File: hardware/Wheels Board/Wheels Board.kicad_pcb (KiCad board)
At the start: 2 copper layers, 224.7 x 101.3 mm, 45 parts, among them J1 Conn_01x05, J10 gnd, J2 24v, J3 Conn_01x03, J4 53307-2471, J5 Conn_01x02, J6 Conn_01x05_Pin, J7 Conn_01x07, J8 Conn_01x03, J9 5v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

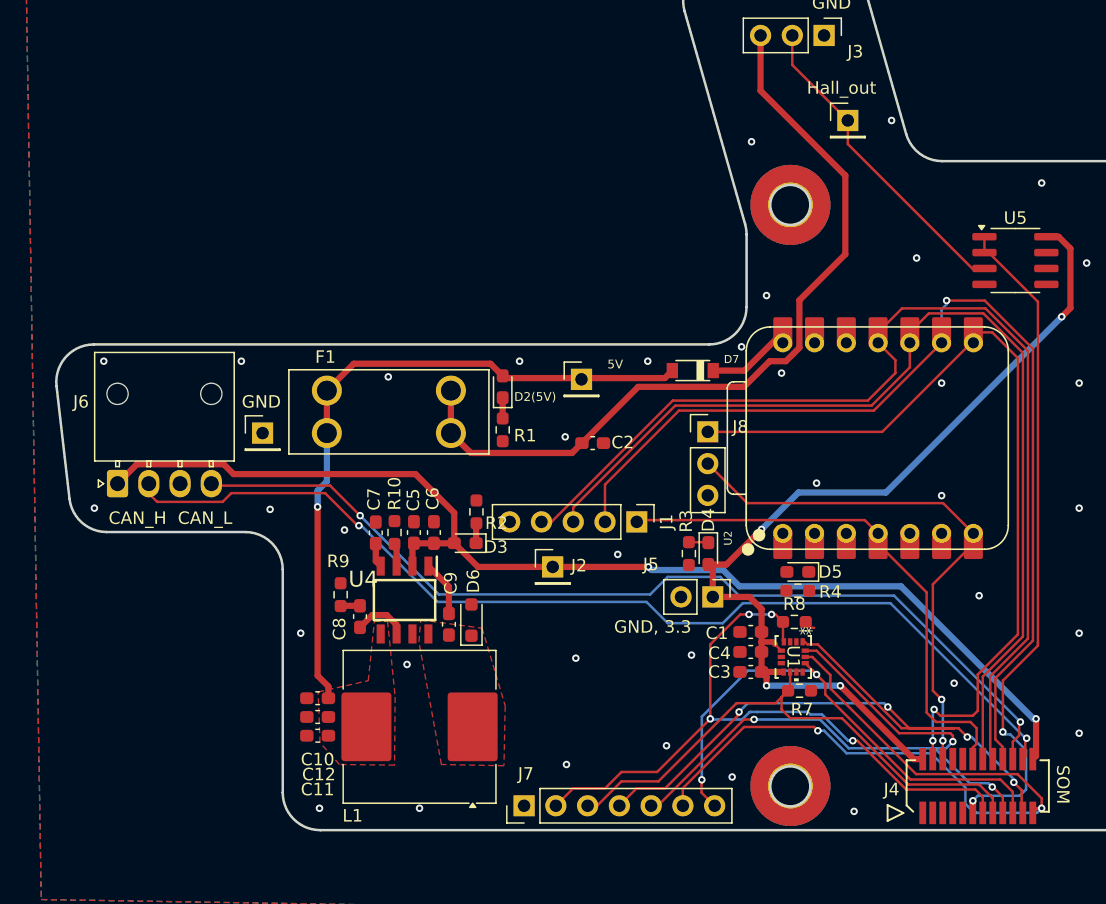
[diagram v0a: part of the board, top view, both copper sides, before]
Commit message: silkscreen final
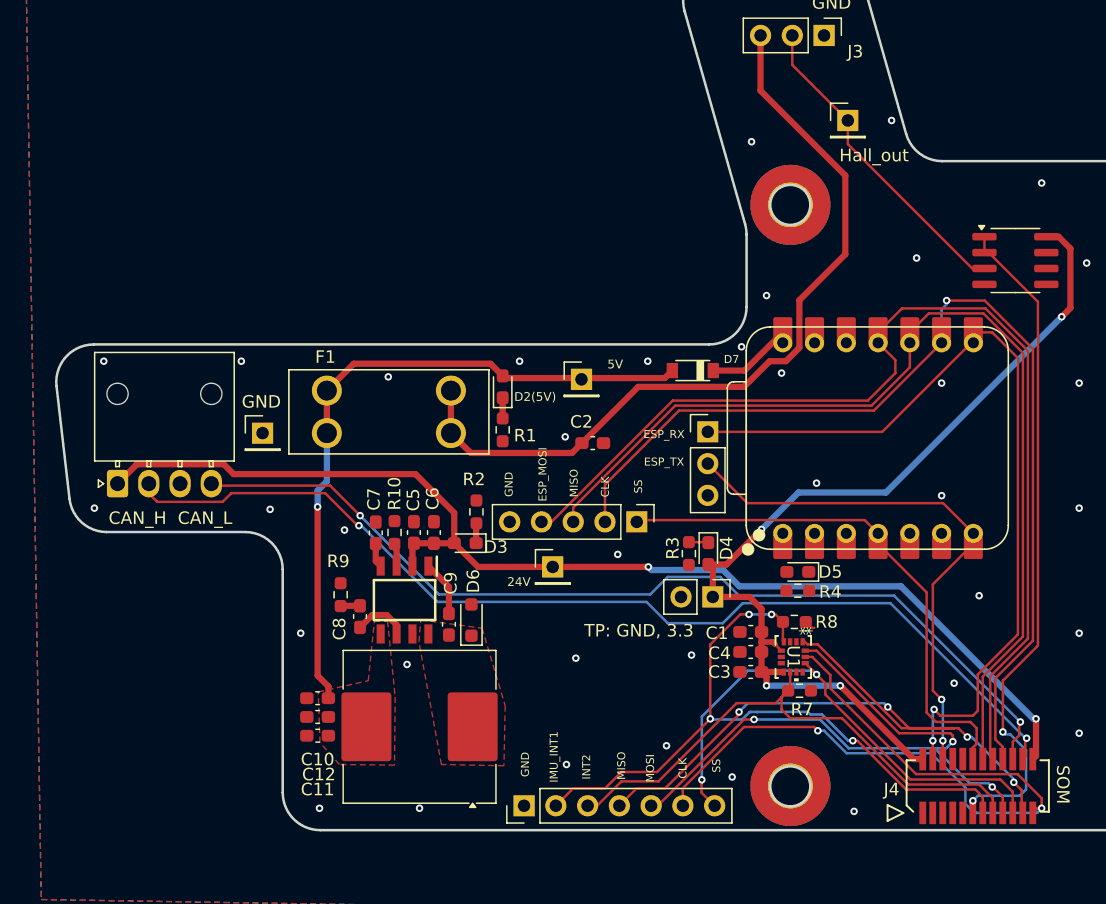
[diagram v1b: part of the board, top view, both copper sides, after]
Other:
- board text added: "24V"
- board text added: "CLK"
- board text added: "ESP_MOSI"
- board text added: "ESP_RX"
- board text added: "ESP_TX"
- board text added: "IMU_INT1"
- board text added: "INT2"
- board text added: "MISO"
- board text added: "MOSI"
- board text added: "SS"
- board text added: "TP: GND, 3.3"
- board text removed: "GND, 3.3"
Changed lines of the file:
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@@
 		(tags "Through hole pin header THT 1x01 2.54mm single row")
 		(property "Reference" "Hall_out"
-			(at -0.5 -2.6 0)
+			(at 2.1 2.8 0)
 			(layer "F.SilkS")
 			(effects
@@
 		(tags "resistor handsolder")
 		(property "Reference" "R2"
-			(at -0.9 1.6 0)
+			(at 2.6 -0.2 0)
 			(layer "F.SilkS")
 			(effects
@@
 			(at 2.55 0.14 180)
 			(layer "F.SilkS")
+			(hide yes)
 			(effects
 				(font
@@
 			(at 6.54 -2.92 180)
 			(layer "F.SilkS")
+			(hide yes)
 			(effects
 				(font
@@
 			(at 2.1 -0.1 0)
 			(layer "F.SilkS")
+			(hide yes)
 			(effects
 				(font
@@
 			(at -2.6 4.95 180)
 			(layer "F.SilkS")
+			(hide yes)
 			(effects
 				(font
@@
 			(unlocked yes)
 			(layer "F.SilkS")
+			(hide yes)
 			(effects
 				(font
@@
 			(at -1.6625 3.300002 180)
 			(layer "F.SilkS")
+			(hide yes)
 			(effects
 				(font
@@
 		(tags "capacitor handsolder")
 		(property "Reference" "C2"
-			(at 2.4 -0.05 0)
+			(at -0.9 -1.7 0)
 			(layer "F.SilkS")
 			(effects
@@
 		(tags "resistor handsolder")
 		(property "Reference" "R8"
-			(at 0 -1.43 0)
+			(at 2.575001 0 0)
 			(layer "F.SilkS")
 			(effects
@@
 			(at 0 -3.4 0)
 			(layer "F.SilkS")
+			(hide yes)
 			(effects
 				(font
@@
 			(at 0 -2.38 90)
 			(layer "F.SilkS")
+			(hide yes)
 			(effects
 				(font
@@
 			(at 2.6 -0.4 0)
 			(layer "F.SilkS")
+			(hide yes)
 			(effects
 				(font
@@
 			(at 5.349999 -7.112501 180)
 			(layer "F.SilkS")
+			(hide yes)
 			(effects
 				(font
@@
 		(tags "resistor handsolder")
 		(property "Reference" "R3"
-			(at -2.594795 0.219267 90)
+			(at -0.435177 1.288604 90)
 			(layer "F.SilkS")
 			(effects
@@
 		(tags "LED handsolder")
 		(property "Reference" "D4"
-			(at -2.687006 0 90)
+			(at -0.435177 -1.455761 90)
 			(layer "F.SilkS")
 			(effects
@@
 		(layer "Edge.Cuts")
 	)
+	(gr_text "ESP_TX\n"
+		(at 101.8 76.3 0)
+		(layer "F.SilkS")
+		(effects
+			(font
+				(size 0.640597 0.640597)
+				(thickness 0.15)
+			)
+		)
+	)
 	(gr_text "5V"
 		(at 97.9 68.5 0)
@@
 	)
 	(gr_text "GND\n"
+		(at 89.4 78.1 90)
+		(layer "F.SilkS")
+		(effects
+			(font
+				(size 0.640597 0.640597)
+				(thickness 0.15)
+			)
+		)
+	)
+	(gr_text "GND\n"
 		(at 115.2 39.6 0)
 		(layer "F.SilkS")
@@
 		)
 	)
+	(gr_text "CLK"
+		(at 103.3 100.8 90)
+		(layer "F.SilkS")
+		(effects
+			(font
+				(size 0.640597 0.640597)
+				(thickness 0.15)
+			)
+		)
+	)
+	(gr_text "CLK\n"
+		(at 97.1 78.3 90)
+		(layer "F.SilkS")
+		(effects
+			(font
+				(size 0.640597 0.640597)
+				(thickness 0.15)
+			)
+		)
+	)
+	(gr_text "MOSI\n"
+		(at 100.7 100.8 90)
+		(layer "F.SilkS")
+		(effects
+			(font
+				(size 0.640597 0.640597)
+				(thickness 0.15)
+			)
+		)
+	)
+	(gr_text "GND\n"
+		(at 90.7 100.5 90)
+		(layer "F.SilkS")
+		(effects
+			(font
+				(size 0.640597 0.640597)
+				(thickness 0.15)
+			)
+		)
+	)
+	(gr_text "MISO\n"
+		(at 94.6 78 90)
+		(layer "F.SilkS")
+		(effects
+			(font
+				(size 0.640597 0.640597)
+				(thickness 0.15)
+			)
+		)
+	)
+	(gr_text "INT2"
+		(at 95.6 100.7 90)
+		(layer "F.SilkS")
+		(effects
+			(font
+				(size 0.640597 0.640597)
+				(thickness 0.15)
+			)
+		)
+	)
 	(gr_text "HALL"
 		(at 111.6 38.5 0)
@@
 		)
 	)
+	(gr_text "IMU_INT1\n"
+		(at 93 99.9 90)
+		(layer "F.SilkS")
+		(effects
+			(font
+				(size 0.640597 0.640597)
+				(thickness 0.15)
+			)
+		)
+	)
+	(gr_text "24V\n"
+		(at 90.2 85.9 0)
+		(layer "F.SilkS")
+		(effects
+			(font
+				(size 0.7 0.7)
+				(thickness 0.15)
+			)
+		)
+	)
+	(gr_text "SS"
+		(at 99.749133 78.268886 90)
+		(layer "F.SilkS")
+		(effects
+			(font
+				(size 0.640597 0.640597)
+				(thickness 0.15)
+			)
+		)
+	)
+	(gr_text "SS\n"
+		(at 106 100.6 90)
+		(layer "F.SilkS")
+		(effects
+			(font
+				(size 0.640597 0.640597)
+				(thickness 0.15)
+			)
+		)
+	)
+	(gr_text "MISO\n"
+		(at 98.4 100.6 90)
+		(layer "F.SilkS")
+		(effects
+			(font
+				(size 0.640597 0.640597)
+				(thickness 0.15)
+			)
+		)
+	)
+	(gr_text "ESP_RX\n"
+		(at 101.8 74.1 0)
+		(layer "F.SilkS")
+		(effects
+			(font
+				(size 0.640597 0.640597)
+				(thickness 0.15)
+			)
+		)
+	)
+	(gr_text "ESP_MOSI\n"
+		(at 92.1 77.3 90)
+		(layer "F.SilkS")
+		(effects
+			(font
+				(size 0.640597 0.640597)
+				(thickness 0.15)
+			)
+		)
+	)
 	(gr_text "CAN_L"
 		(at 65.1 80.8 0)
@@
 		)
 	)
-	(gr_text "GND, 3.3"
-		(at 100.9 89.5 0)
+	(gr_text "TP: GND, 3.3"
+		(at 99.8 89.8 0)
 		(layer "F.SilkS")
 		(effects
@@
 		(name "$teardrop_padvia$")
 		(hatch none 0.1)
-		(priority 30009)
+		(priority 30000)
 		(attr
 			(teardrop
@@
 		(name "$teardrop_padvia$")
 		(hatch none 0.1)
-		(priority 30010)
+		(priority 30007)
 		(attr
 			(teardrop
@@
 		(polygon
 			(pts
-				(xy 81.935001 83.55) (xy 81.435001 83.55) (xy 81.360001 83.875) (xy 81.685001 84.64) (xy 82.010001 83.875)
+				(xy 82.75 83.0625) (xy 82.75 82.5625) (xy 82.194869 82.3375) (xy 81.799 82.8125) (xy 82.194869 83.2875)
 			)
 		)
 	)
 	(zone
-		(net 3)
-		(net_name "+24V")
+		(net 45)
+		(net_name "/24v to 5v convertor/ROSC")
 		(layer "F.Cu")
 		(name "$teardrop_padvia$")
 		(hatch none 0.1)
-		(priority 30007)
+		(priority 30002)
 		(attr
 			(teardrop
@@
 		(polygon
 			(pts
-				(xy 82.75 83.0625) (xy 82.75 82.5625) (xy 82.194869 82.3375) (xy 81.799 82.8125) (xy 82.194869 83.2875)
+				(xy 80.665001 83.55) (xy 80.165001 83.55) (xy 80.090001 83.875) (xy 80.415001 84.64) (xy 80.740001 83.875)
 			)
 		)
@@
 	)
 	(zone
-		(net 9)
-		(net_name "+5V")
-		(layer "F.Cu")
-		(hatch edge 0.5)
-		(priority 4)
-		(connect_pads yes
-			(clearance 0.1)
-		)
-		(min_thickness 0.1)
-		(filled_areas_thickness no)
-		(fill yes
-			(thermal_gap 0.1)
-			(thermal_bridge_width 0.5)
-		)
-		(polygon
-			(pts
-				(xy 78.639835 89.05) (xy 79.695 89.05) (xy 80.3 95.1) (xy 80.25 100.55) (xy 75.843032 100.5) (xy 74.293032 98.75)
-				(xy 74.143032 94.7) (xy 78.15 93.8)
-			)
-		)
-	)
-	(zone
 		(net 7)
 		(net_name "Net-(U4-BOOT)")
@@
 		(name "$teardrop_padvia$")
 		(hatch none 0.1)
-		(priority 30012)
+		(priority 30003)
 		(attr
 			(teardrop
@@
 	)
 	(zone
-		(net 45)
-		(net_name "/24v to 5v convertor/ROSC")
+		(net 3)
+		(net_name "+24V")
 		(layer "F.Cu")
 		(name "$teardrop_padvia$")
 		(hatch none 0.1)
-		(priority 30011)
+		(priority 30001)
 		(attr
 			(teardrop
@@
 		(polygon
 			(pts
-				(xy 80.665001 83.55) (xy 80.165001 83.55) (xy 80.090001 83.875) (xy 80.415001 84.64) (xy 80.740001 83.875)
+				(xy 81.935001 83.55) (xy 81.435001 83.55) (xy 81.360001 83.875) (xy 81.685001 84.64) (xy 82.010001 83.875)
+			)
+		)
+	)
+	(zone
+		(net 9)
+		(net_name "+5V")
+		(layer "F.Cu")
+		(hatch edge 0.5)
+		(priority 4)
+		(connect_pads yes
+			(clearance 0.1)
+		)
+		(min_thickness 0.1)
+		(filled_areas_thickness no)
+		(fill yes
+			(thermal_gap 0.1)
+			(thermal_bridge_width 0.5)
+		)
+		(polygon
+			(pts
+				(xy 78.639835 89.05) (xy 79.695 89.05) (xy 80.3 95.1) (xy 80.25 100.55) (xy 75.843032 100.5) (xy 74.293032 98.75)
+				(xy 74.143032 94.7) (xy 78.15 93.8)
 			)
 		)

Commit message: silkscreen final2
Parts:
- removed LOGO1: LHRS, UTSVT_Logos:LHRs_LOGO
- added G***: LOGO, LOGO, F.Cu at (102.7, 91.1)
- moved LOGO2 77.7 mm to (138.4, 73.5), turned to 90 degrees
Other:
- board size 224.7 x 101.3 mm -> 92.9 x 69.7 mm
- board text added: "02/14/26"
- board text added: "Wheels board Rev B <3"

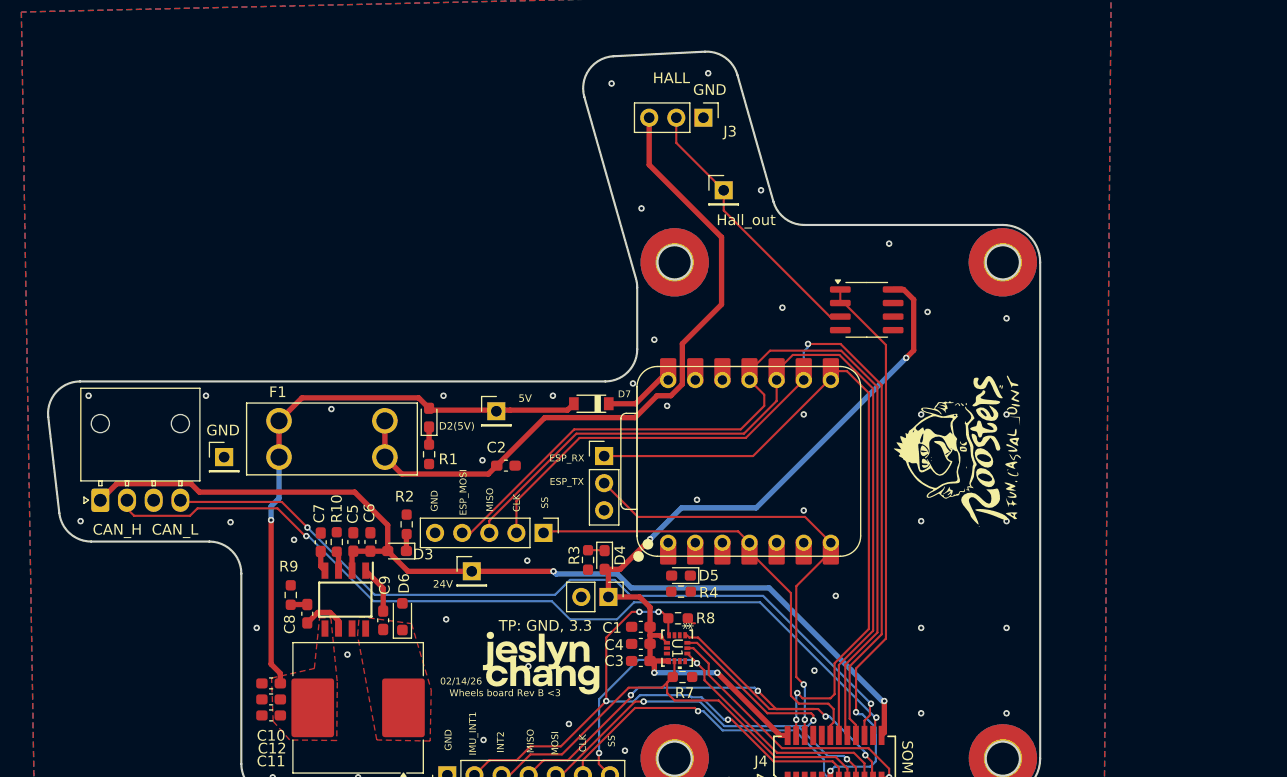
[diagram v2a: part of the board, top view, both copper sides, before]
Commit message: conn changes
rotated can conn, changed hall conn to hor, fixed tp clearance
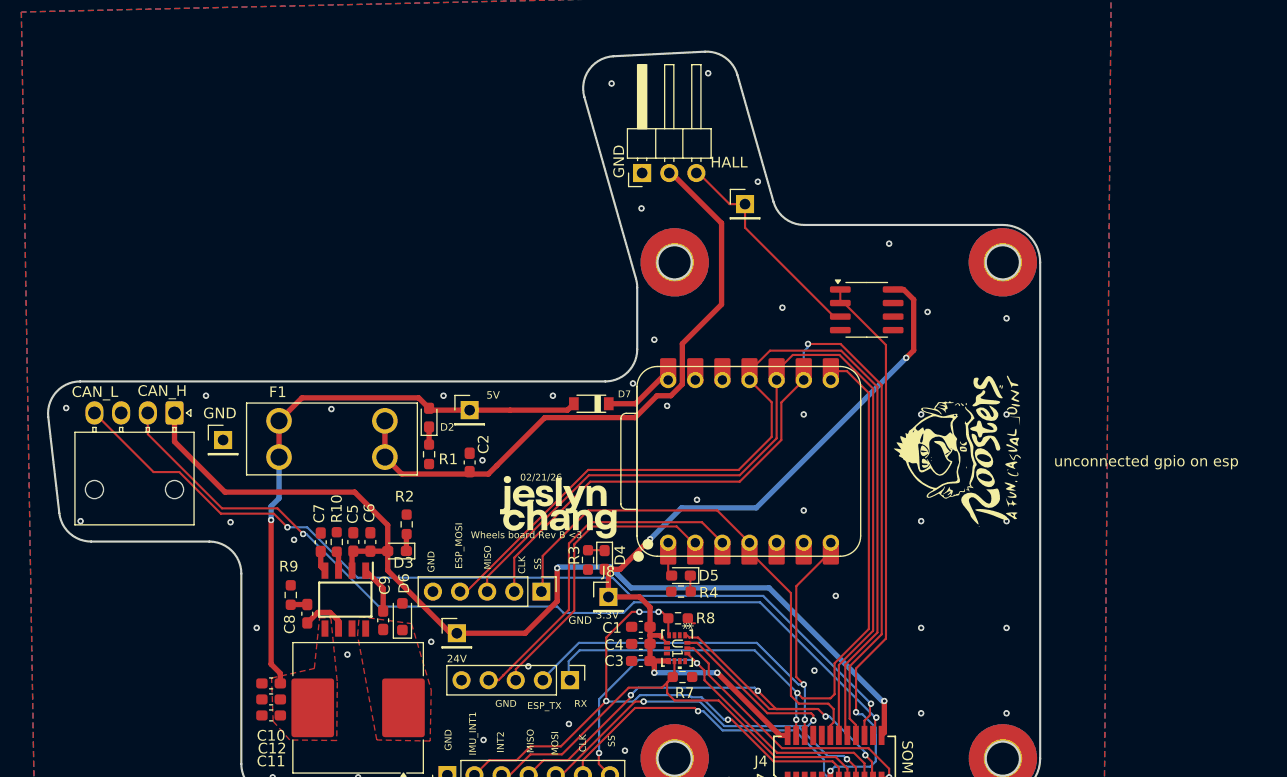
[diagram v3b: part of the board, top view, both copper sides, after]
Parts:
- removed J5: Conn_01x02, Connector_PinHeader_2.54mm:PinHeader_1x02_P2.54mm_Vertical
- added J12: Conn_01x05, Connector_PinHeader_2.54mm:PinHeader_1x05_P2.54mm_Vertical, F.Cu at (102.1, 94.9)
- added LOGO1: LHRS, UTSVT_Logos:LHRs_LOGO, F.Cu at (44.1, 152.7)
- J3: footprint Connector_PinHeader_2.54mm:PinHeader_1x03_P2.54mm_Vertical -> Connector_PinHeader_2.54mm:PinHeader_1x03_P2.54mm_Horizontal
- J8: value Conn_01x03 -> 24v; footprint Connector_PinHeader_2.54mm:PinHeader_1x03_P2.54mm_Vertical -> Connector_PinHeader_2.54mm:PinHeader_1x01_P2.54mm_Vertical
- moved G*** 14.7 mm to (104.3, 76.5)
- moved J8 13.2 mm to (105.7, 87.1)
- moved J6 10.7 mm to (65.0, 69.9), turned to -90 degrees
- moved J3 7.74 mm to (108.9, 47.4), turned to 90 degrees
- moved J2 5.97 mm to (91.5, 90.5)
- moved J1 5.50 mm to (99.4, 86.6)
- moved C2 3.41 mm to (92.7, 74.5), turned to 90 degrees
- moved J9 2.50 mm to (92.7, 69.6)
- moved J11 2.39 mm to (118.5, 50.3)
- moved J10 1.60 mm to (69.6, 72.4)
- renumbered D2(5V) to D2, Hall_out to J11
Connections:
- C2 pad 1: Net-(J3-Pin_3) -> Net-(J3-Pin_2)
- F1 pad 2: Net-(J3-Pin_3) -> Net-(J3-Pin_2)
- J3 pad 2: /HALL_OUT -> Net-(J3-Pin_2)
- J3 pad 3: Net-(J3-Pin_3) -> /HALL_OUT
- J4 pad 7: /EXTRA_GPIO1 -> unconnected-(J4-OPAMP1_VINP-Pad7)
- J4 pad 9: /EXTRA_GPIO2 -> unconnected-(J4-ADC1_IN7-Pad9)
- J8 pad 1: /ESP_UART_RX -> +3.3V
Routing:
- net Net-(J3-Pin_3): track 64.7 -> 0.00 mm
- net Net-(J3-Pin_2): track 0.00 -> 58.9 mm
- net /EXTRA_GPIO2: track 0.00 -> 32.5 mm
- net /EXTRA_GPIO1: track 0.00 -> 29.2 mm
- net /CAN_L: track 77.2 -> 87.3 mm
- net /ESP_SPI_SS: track 42.0 -> 48.0 mm
- net /ESP_SPI_MOSI: track 84.4 -> 89.6 mm
- net /HALL_OUT: track 25.6 -> 20.4 mm
- net +24V: track 92.4 -> 97.1 mm
- net /ESP_SPI_MISO: track 79.5 -> 84.1 mm
- net /ESP_SPI_CLK: track 80.9 -> 85.6 mm
- net /ESP_UART_TX: track 42.4 -> 46.5 mm
- net /XIAO_HEARTBEAT_LED: track 0.00 -> 2.38 mm
- net /CAN_H: track 82.0 -> 83.9 mm
- net Net-(D5-K): track 0.00 -> 1.52 mm
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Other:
- board text added: "02/21/26"
- board text added: "3.3V"
- board text added: "RX"
- board text added: "unconnected gpio on esp"
- board text removed: "02/14/26"
- board text removed: "ESP_RX"
- board text removed: "TP: GND, 3.3"
